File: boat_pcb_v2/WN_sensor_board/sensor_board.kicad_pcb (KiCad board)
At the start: 4 copper layers, 0.7 x 0.5 mm, 120 parts, among them J1 MSD-4-A, J10 PPTC031LFBN-RC, J11 RFPC-SMA28-F, J12 PPTC031LFBN-RC, J13 PPTC031LFBN-RC, J14 RFPC-SMA28-F, J15 USB4120-03-C_REVA6, J16 USB4120-03-C_REVA6, J17 PPTC031LFBN-RC, J18 PPTC031LFBN-RC, J2 RFPC-SMA28-F, J20 TSW-108-07-F-D, J21 TSW-108-07-F-D, J22 TSW-108-07-F-D, J3 RFPC-SMA28-F, J4 RFPC-SMA28-F, J5 PPTC031LFBN-RC, J6 PPTC031LFBN-RC, J7 PPTC031LFBN-RC, J8 PPTC031LFBN-RC, J9 PPTC031LFBN-RC, U1 MAX14933ASE_T, U16 BSS123-7-F, U17 BSS123-7-F, U18 BSS123-7-F, U19 BSS123-7-F, U2 ESP32-S3-WROOM-1-N8, U3 MCP2200-I_SO, U4 AP62301WU-7, U5 MAX14933ASE_T, U6 MAX14933ASE_T, U7 MAX14933ASE_T, U8 BSS123-7-F, U9 BSS123-7-F, Y1 ECS-120-12-33-AGN-TR

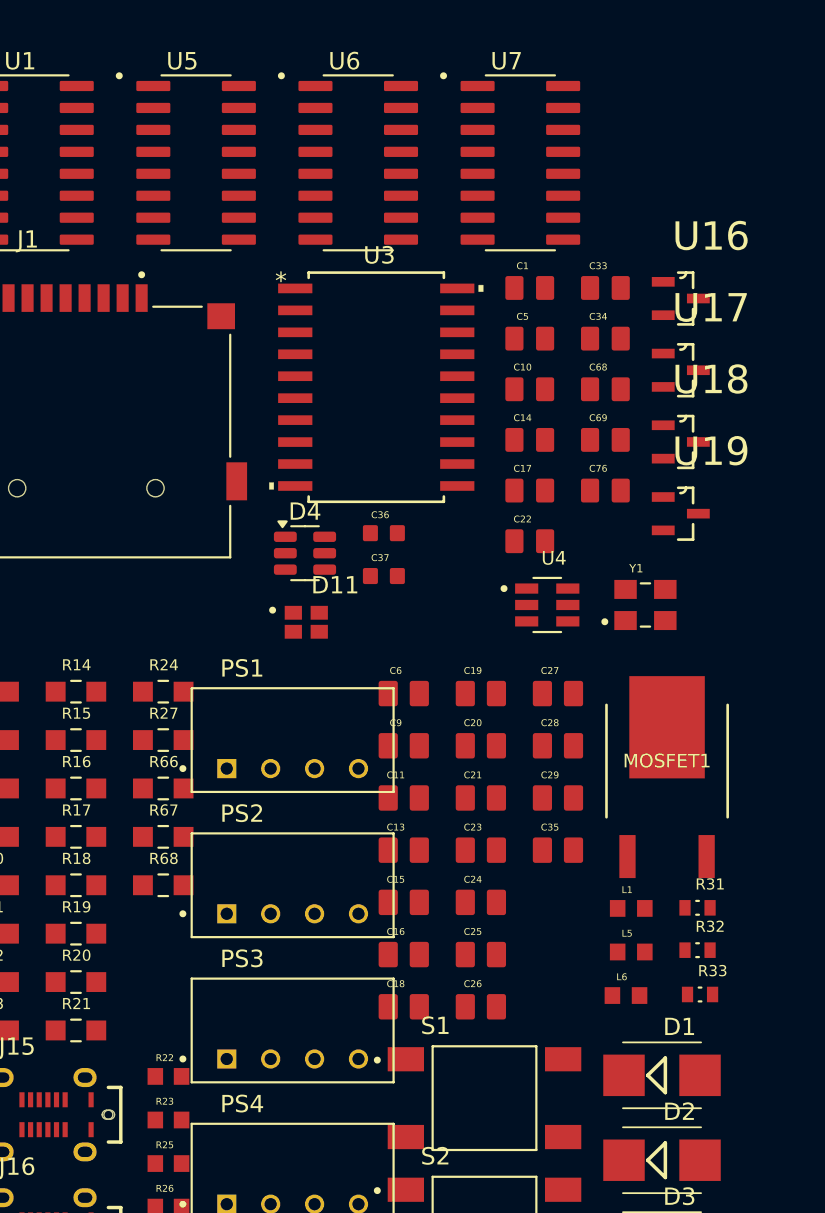
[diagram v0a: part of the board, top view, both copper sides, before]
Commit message: fixed some footprints
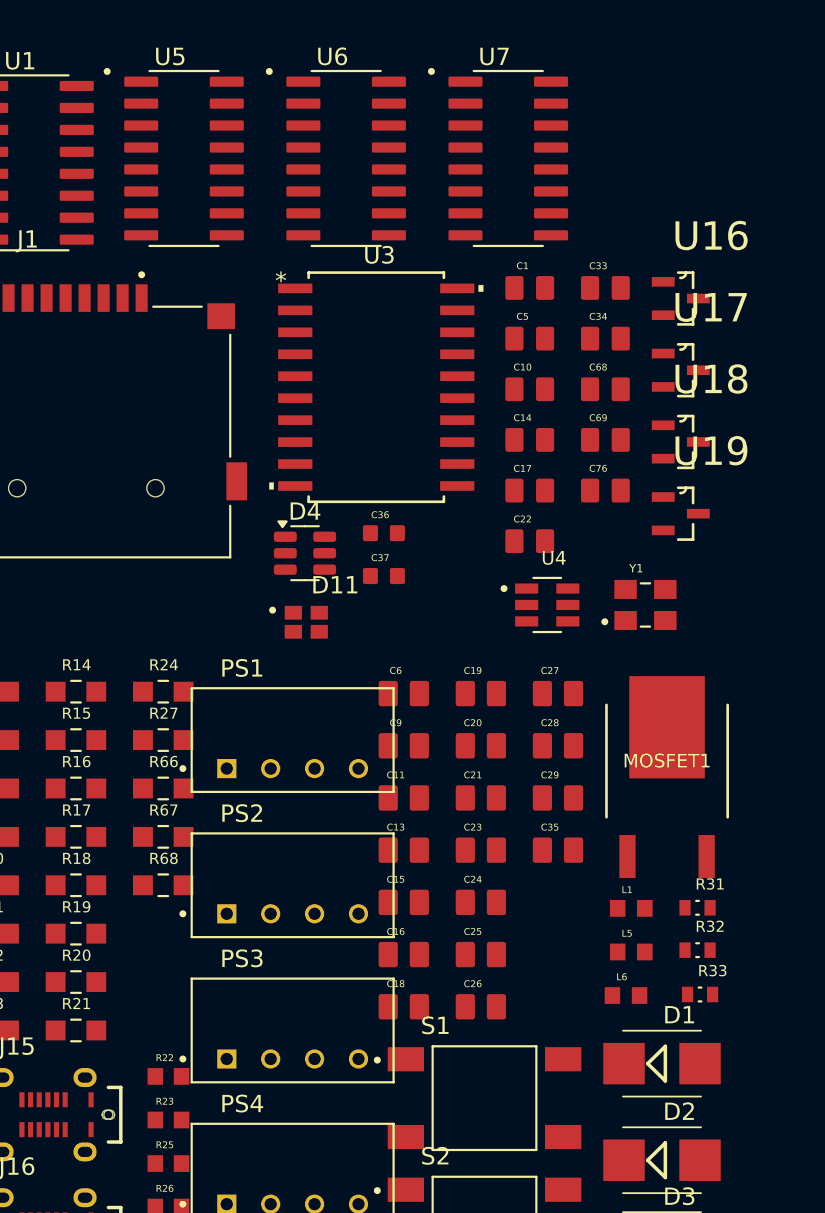
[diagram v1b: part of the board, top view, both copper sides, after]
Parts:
- moved U5 0.74 mm to (124.1, 46.1)
- moved U6 0.74 mm to (133.5, 46.1)
- moved U7 0.74 mm to (142.9, 46.1)
- moved D1 0.68 mm to (151.8, 98.5)
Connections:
- net /ISO_3V3 renamed +ISO_3V3
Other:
- rule pad_to_mask_clearance: 0 -> 0.1

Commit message: minor updates related to board layout
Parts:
- D1, D2, D3, D4, J1, U1, U3, U4, U5, U6, U7, Y1: moved to B.Cu
- moved U2 87.2 mm to (57.0, 130.0)
- moved J20 28.8 mm to (178.3, 53.3), turned to 90 degrees
- turned D1 to 180 degrees
- turned D2 to 180 degrees
- turned D3 to 180 degrees
- turned D4 to 180 degrees
- turned J1 to 180 degrees
- turned U1 to 180 degrees
- turned U3 to 180 degrees
- turned U4 to 180 degrees
- turned U5 to 180 degrees
- turned U6 to 180 degrees
- turned U7 to 180 degrees
- turned Y1 to 180 degrees
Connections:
- J22 pad 01: unconnected-(J22-Pad01) -> /IO1
- J22 pad 02: unconnected-(J22-Pad02) -> /IO40
- J22 pad 03: unconnected-(J22-Pad03) -> /IO2
- J22 pad 04: unconnected-(J22-Pad04) -> /IO41
- J22 pad 05: unconnected-(J22-Pad05) -> /IO3
- J22 pad 06: unconnected-(J22-Pad06) -> /IO42
- J22 pad 07: unconnected-(J22-Pad07) -> /IO6
- J22 pad 08: unconnected-(J22-Pad08) -> /IO47
- J22 pad 09: unconnected-(J22-Pad09) -> /IO7
- J22 pad 10: unconnected-(J22-Pad10) -> /IO48
- J22 pad 11: unconnected-(J22-Pad11) -> /IO17
- J22 pad 12: unconnected-(J22-Pad12) -> +3V3
- J22 pad 13: unconnected-(J22-Pad13) -> /IO18
- J22 pad 14: unconnected-(J22-Pad14) -> +3V3
- J22 pad 15: unconnected-(J22-Pad15) -> GND
- J22 pad 16: unconnected-(J22-Pad16) -> +3V3
- U2 pad 10: unconnected-(U2-IO17-Pad10) -> /IO17
- U2 pad 11: unconnected-(U2-IO18-Pad11) -> /IO18
- U2 pad 15: unconnected-(U2-IO3-Pad15) -> /IO3
- U2 pad 24: unconnected-(U2-IO47-Pad24) -> /IO47
- U2 pad 25: unconnected-(U2-IO48-Pad25) -> /IO48
- U2 pad 33: unconnected-(U2-IO40-Pad33) -> /IO40
- U2 pad 34: unconnected-(U2-IO41-Pad34) -> /IO41
- U2 pad 35: unconnected-(U2-IO42-Pad35) -> /IO42
- U2 pad 6: unconnected-(U2-IO6-Pad6) -> /IO6
- U2 pad 7: unconnected-(U2-IO7-Pad7) -> /IO7
